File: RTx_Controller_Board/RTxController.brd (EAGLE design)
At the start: 101.6 x 85.5 mm, 73 parts

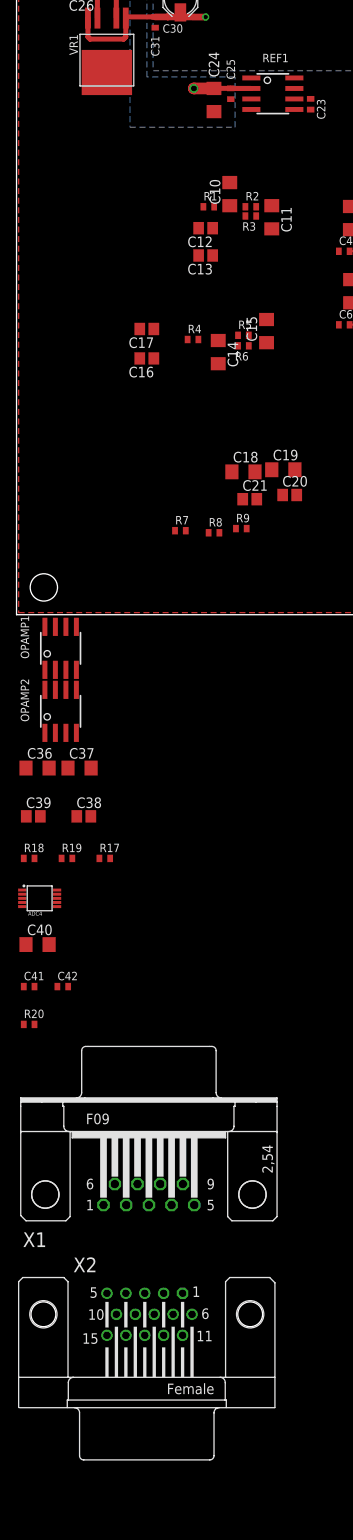
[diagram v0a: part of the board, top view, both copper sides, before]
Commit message: Changed ARef to 5.000V.
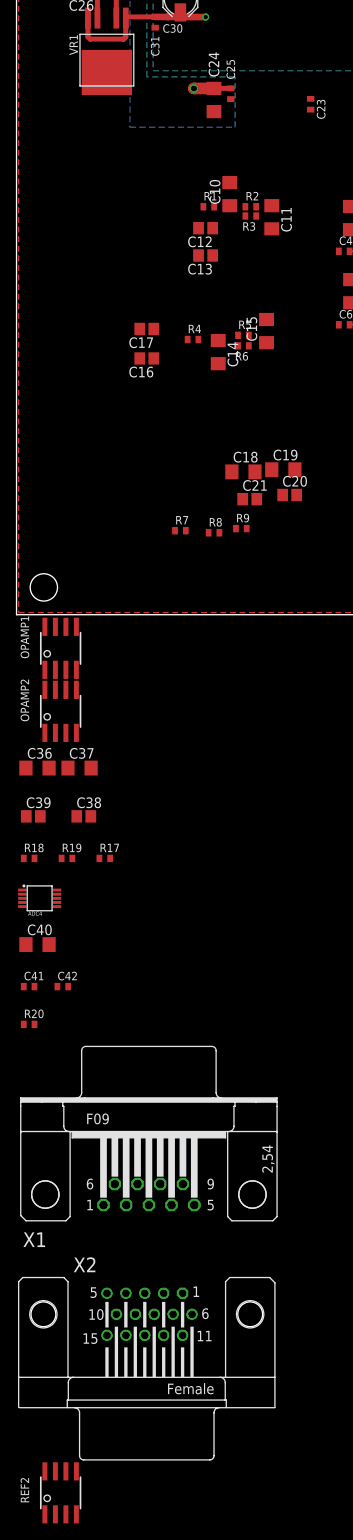
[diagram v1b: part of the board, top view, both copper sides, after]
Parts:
- removed REF1: ADR433RM-8, motorFeedback:SOIC8
- added REF2: ADR435RM-8, motorFeedback:SOIC8
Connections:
- removed net +3.000VREF: ADC1.1, ADC2.1, ADC3.1, ADC4.1, C1.2, C2.2, C23.1, C3.2, C40.2, R10.1, REF1.6
- new net +18V: C24.1, C25.1, REF2.2
- new net +5.000VREF: ADC1.1, ADC2.1, ADC3.1, ADC4.1, C1.2, C2.2, C23.1, C3.2, C40.2, R10.1, REF2.6
- net +5V: no longer C24.1, C25.1, REF1.2
- net GND: now also REF2.4; no longer REF1.4
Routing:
- net +5.000VREF: track 0.00 -> 7.47 mm
- net +3.000VREF: track 7.47 -> 0.00 mm
- net +5V: track 14.1 -> 7.19 mm, vias 2 -> 1
- net +18V: track 0.00 -> 4.49 mm, vias 0 -> 1
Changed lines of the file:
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@@
 <attribute name="NAME" x="42.796" y="42.858" size="0.5" layer="25" font="vector"/>
 </element>
-<element name="REF1" library="motorFeedback" package="SOIC8" value="ADR433RM-8" x="30.988" y="62.992" rot="R270"/>
 <element name="ADC2" library="motorFeedback" package="MSOP-10" value="AD7685RM-10" x="44.196" y="36.068"/>
 <element name="ADC3" library="motorFeedback" package="MSOP-10" value="AD7685RM-10" x="48.26" y="11.684"/>
@@
 <attribute name="OC_FARNELL" value="unknown" x="15.748" y="-84.582" size="1.778" layer="27" display="off"/>
 </element>
+<element name="REF2" library="motorFeedback" package="SOIC8" value="ADR435RM-8" x="5.334" y="-106.172"/>
 </elements>
 <signals>
@@
 <contactref element="ADC1" pad="4"/>
 <contactref element="ADC1" pad="5"/>
-<contactref element="REF1" pad="4"/>
 <contactref element="ADC2" pad="4"/>
 <contactref element="ADC2" pad="5"/>
@@
 <contactref element="ADC4" pad="5"/>
 <contactref element="ADC4" pad="4"/>
+<contactref element="REF2" pad="4"/>
 <wire x1="88.9" y1="59.944" x2="93.472" y2="63.83" width="0" layer="19" extent="1-1"/>
 <wire x1="88.9" y1="58.42" x2="88.9" y2="59.944" width="0" layer="19" extent="1-1"/>
@@
 <wire x1="46.228" y1="60.618" x2="74.676" y2="63.83" width="0" layer="19" extent="1-1"/>
 <wire x1="35.56" y1="61.072" x2="46.228" y2="60.618" width="0" layer="19" extent="1-1"/>
-<wire x1="28.388" y1="61.087" x2="35.56" y2="61.072" width="0" layer="19" extent="1-1"/>
-<wire x1="25.908" y1="62.342" x2="28.388" y2="61.087" width="0" layer="19" extent="1-1"/>
+<wire x1="25.908" y1="62.342" x2="35.56" y2="61.072" width="0" layer="19" extent="1-1"/>
 <wire x1="23.876" y1="60.83" x2="25.908" y2="62.342" width="0" layer="19" extent="1-1"/>
 <wire x1="25.781" y1="52.2508" x2="23.876" y2="60.83" width="0" layer="19" extent="1-1"/>
@@
 <wire x1="2.174" y1="-44.958" x2="1.14" y2="-39.878" width="0" layer="19" extent="1-1"/>
 <wire x1="6.238" y1="-44.958" x2="2.174" y2="-44.958" width="0" layer="19" extent="1-1"/>
+<wire x1="7.239" y1="-108.772" x2="6.238" y2="-44.958" width="0" layer="19" extent="1-1"/>
 </signal>
 <signal name="+5V">
 <contactref element="ADC1" pad="2"/>
-<contactref element="REF1" pad="2"/>
 <contactref element="C4" pad="1"/>
 <contactref element="C6" pad="1"/>
 <contactref element="C8" pad="1"/>
-<contactref element="C25" pad="1"/>
-<contactref element="C24" pad="1"/>
 <contactref element="VR1" pad="4"/>
 <contactref element="C26" pad="1"/>
@@
 <wire x1="9.779" y1="75.438" x2="9.54" y2="75.677" width="0.6096" layer="1" curve="-90"/>
 <wire x1="9.54" y1="75.677" x2="9.54" y2="77.597" width="0.6096" layer="1"/>
-<wire x1="23.876" y1="63.63" x2="25.908" y2="63.642" width="0.6096" layer="1"/>
-<wire x1="25.908" y1="63.642" x2="25.923" y2="63.627" width="0.6096" layer="1"/>
-<wire x1="25.923" y1="63.627" x2="28.388" y2="63.627" width="0.6096" layer="1"/>
-<wire x1="21.4406" y1="63.63" x2="23.876" y2="63.63" width="1.4224" layer="1"/>
-<wire x1="21.4376" y1="63.627" x2="21.4406" y2="63.63" width="1.4224" layer="1"/>
 <wire x1="9.54" y1="77.597" x2="9.54" y2="78.9536" width="0.6096" layer="1"/>
 <wire x1="9.54" y1="78.9536" x2="9.525" y2="78.9686" width="0.6096" layer="1"/>
-<via x="21.4376" y="63.627" extent="1-16" drill="0.7"/>
 <via x="9.525" y="78.9686" extent="1-16" drill="0.6"/>
 <polygon width="0.254" layer="16">
@@
 <wire x1="42.096" y1="36.568" x2="38.974" y2="43.942" width="0" layer="19" extent="1-1"/>
 <wire x1="38.974" y1="35.052" x2="42.096" y2="36.568" width="0" layer="19" extent="1-1"/>
-<wire x1="28.388" y1="63.627" x2="38.974" y2="43.942" width="0" layer="19" extent="1-1"/>
-<wire x1="9.779" y1="72.136" x2="21.4406" y2="63.63" width="0" layer="19" extent="1-1"/>
 <wire x1="46.16" y1="12.184" x2="38.974" y2="35.052" width="0" layer="19" extent="1-1"/>
 <wire x1="43.038" y1="10.668" x2="46.16" y2="12.184" width="0" layer="19" extent="1-1"/>
+<wire x1="9.779" y1="72.136" x2="38.974" y2="43.942" width="0" layer="19" extent="1-1"/>
 <wire x1="3.429" y1="-1.464" x2="43.038" y2="10.668" width="0" layer="19" extent="1-1"/>
 <wire x1="0.694" y1="-33.79" x2="3.429" y2="-1.464" width="0" layer="19" extent="1-1"/>
 <wire x1="0.874" y1="-44.958" x2="0.694" y2="-33.79" width="0" layer="19" extent="1-1"/>
-</signal>
-<signal name="+3.000VREF">
-<contactref element="ADC1" pad="1"/>
-<contactref element="ADC2" pad="1"/>
-<contactref element="ADC3" pad="1"/>
-<contactref element="C1" pad="2"/>
-<contactref element="C2" pad="2"/>
-<contactref element="C3" pad="2"/>
-<contactref element="REF1" pad="6"/>
-<contactref element="R10" pad="1"/>
-<contactref element="C23" pad="1"/>
-<wire x1="40.386" y1="37.068" x2="42.096" y2="37.068" width="0.254" layer="1"/>
-<wire x1="40.386" y1="37.716" x2="40.386" y2="37.068" width="0.254" layer="1"/>
-<wire x1="44.45" y1="12.684" x2="46.16" y2="12.684" width="0.254" layer="1"/>
-<wire x1="44.45" y1="12.684" x2="44.45" y2="13.332" width="0.254" layer="1"/>
-<wire x1="40.402" y1="45.958" x2="42.096" y2="45.958" width="0.254" layer="1"/>
-<wire x1="40.386" y1="45.974" x2="40.402" y2="45.958" width="0.254" layer="1"/>
-<wire x1="40.386" y1="46.7838" x2="40.386" y2="45.974" width="0.254" layer="1"/>
-<wire x1="40.3606" y1="46.5552" x2="40.386" y2="46.7838" width="0.254" layer="1"/>
-<contactref element="C40" pad="2"/>
-<contactref element="ADC4" pad="1"/>
-<wire x1="35.56" y1="62.372" x2="42.9872" y2="62.357" width="0" layer="19" extent="1-1"/>
-<wire x1="33.588" y1="62.357" x2="35.56" y2="62.372" width="0" layer="19" extent="1-1"/>
-<wire x1="40.386" y1="46.7838" x2="42.9872" y2="62.357" width="0" layer="19" extent="1-1"/>
-<wire x1="40.386" y1="37.716" x2="40.402" y2="45.958" width="0" layer="19" extent="1-1"/>
-<wire x1="44.45" y1="13.332" x2="42.096" y2="37.068" width="0" layer="19" extent="1-1"/>
-<wire x1="0.694" y1="-33.29" x2="44.45" y2="12.684" width="0" layer="19" extent="1-1"/>
-<wire x1="3.94" y1="-39.878" x2="0.694" y2="-33.29" width="0" layer="19" extent="1-1"/>
 </signal>
 <signal name="CNV">
@@
 <wire x1="4.894" y1="-34.79" x2="0.874" y2="-49.53" width="0" layer="19" extent="1-1"/>
 </signal>
+<signal name="+5.000VREF">
+<contactref element="R10" pad="1"/>
+<contactref element="C23" pad="1"/>
+<contactref element="ADC1" pad="1"/>
+<contactref element="C1" pad="2"/>
+<wire x1="40.402" y1="45.958" x2="42.096" y2="45.958" width="0.254" layer="1"/>
+<wire x1="40.386" y1="45.974" x2="40.402" y2="45.958" width="0.254" layer="1"/>
+<wire x1="40.386" y1="46.7838" x2="40.386" y2="45.974" width="0.254" layer="1"/>
+<wire x1="40.3606" y1="46.5552" x2="40.386" y2="46.7838" width="0.254" layer="1"/>
+<contactref element="ADC2" pad="1"/>
+<contactref element="C2" pad="2"/>
+<wire x1="40.386" y1="37.068" x2="42.096" y2="37.068" width="0.254" layer="1"/>
+<wire x1="40.386" y1="37.716" x2="40.386" y2="37.068" width="0.254" layer="1"/>
+<contactref element="ADC3" pad="1"/>
+<contactref element="C3" pad="2"/>
+<wire x1="44.45" y1="12.684" x2="46.16" y2="12.684" width="0.254" layer="1"/>
+<wire x1="44.45" y1="12.684" x2="44.45" y2="13.332" width="0.254" layer="1"/>
+<contactref element="C40" pad="2"/>
+<contactref element="ADC4" pad="1"/>
+<contactref element="REF2" pad="6"/>
+<wire x1="35.56" y1="62.372" x2="42.9872" y2="62.357" width="0" layer="19" extent="1-1"/>
+<wire x1="40.386" y1="46.7838" x2="42.9872" y2="62.357" width="0" layer="19" extent="1-1"/>
+<wire x1="40.386" y1="37.716" x2="40.402" y2="45.958" width="0" layer="19" extent="1-1"/>
+<wire x1="44.45" y1="13.332" x2="42.096" y2="37.068" width="0" layer="19" extent="1-1"/>
+<wire x1="0.694" y1="-33.29" x2="44.45" y2="12.684" width="0" layer="19" extent="1-1"/>
+<wire x1="3.94" y1="-39.878" x2="0.694" y2="-33.29" width="0" layer="19" extent="1-1"/>
+<wire x1="5.969" y1="-103.572" x2="3.94" y2="-39.878" width="0" layer="19" extent="1-1"/>
+</signal>
+<signal name="+18V">
+<contactref element="C25" pad="1"/>
+<contactref element="C24" pad="1"/>
+<contactref element="REF2" pad="2"/>
+<wire x1="23.876" y1="63.63" x2="25.908" y2="63.642" width="0.6096" layer="1"/>
+<wire x1="25.908" y1="63.642" x2="25.923" y2="63.627" width="0.6096" layer="1"/>
+<wire x1="21.4406" y1="63.63" x2="23.876" y2="63.63" width="1.4224" layer="1"/>
+<wire x1="21.4376" y1="63.627" x2="21.4406" y2="63.63" width="1.4224" layer="1"/>
+<via x="21.4376" y="63.627" extent="1-16" drill="0.7"/>
+<wire x1="21.4406" y1="63.63" x2="4.699" y2="-108.772" width="0" layer="19" extent="1-1"/>
+</signal>
 </signals>

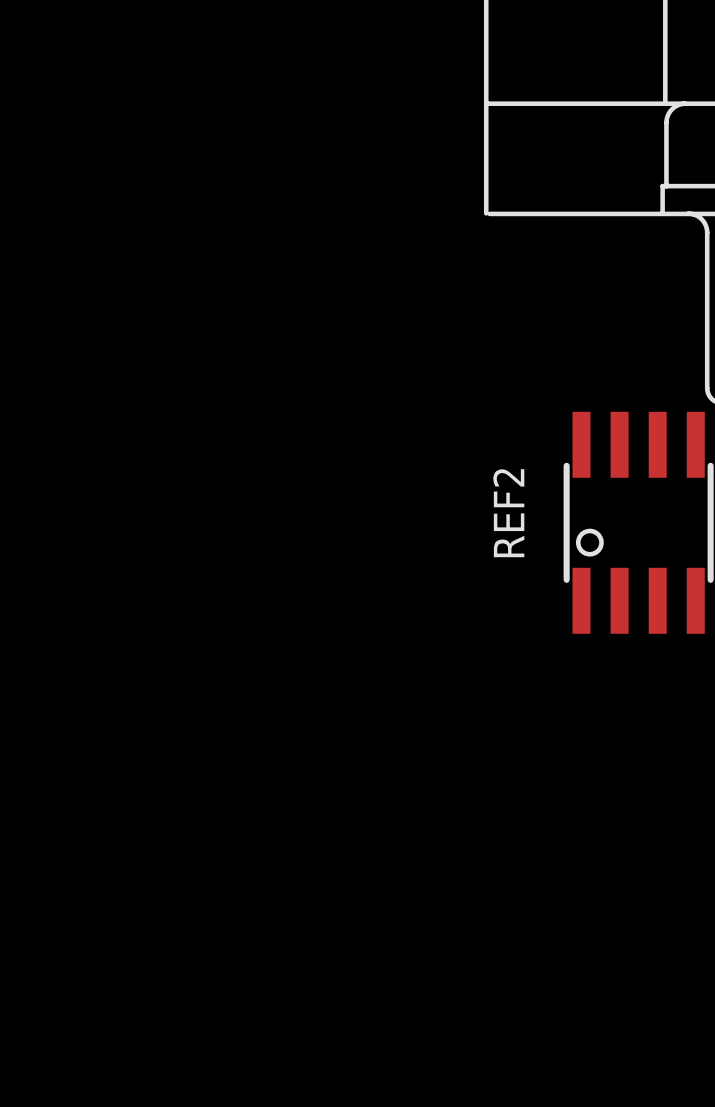
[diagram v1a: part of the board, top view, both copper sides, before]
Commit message: Initial check-in datasheet for USB ESD protection. Added initial USB setup to schematic.
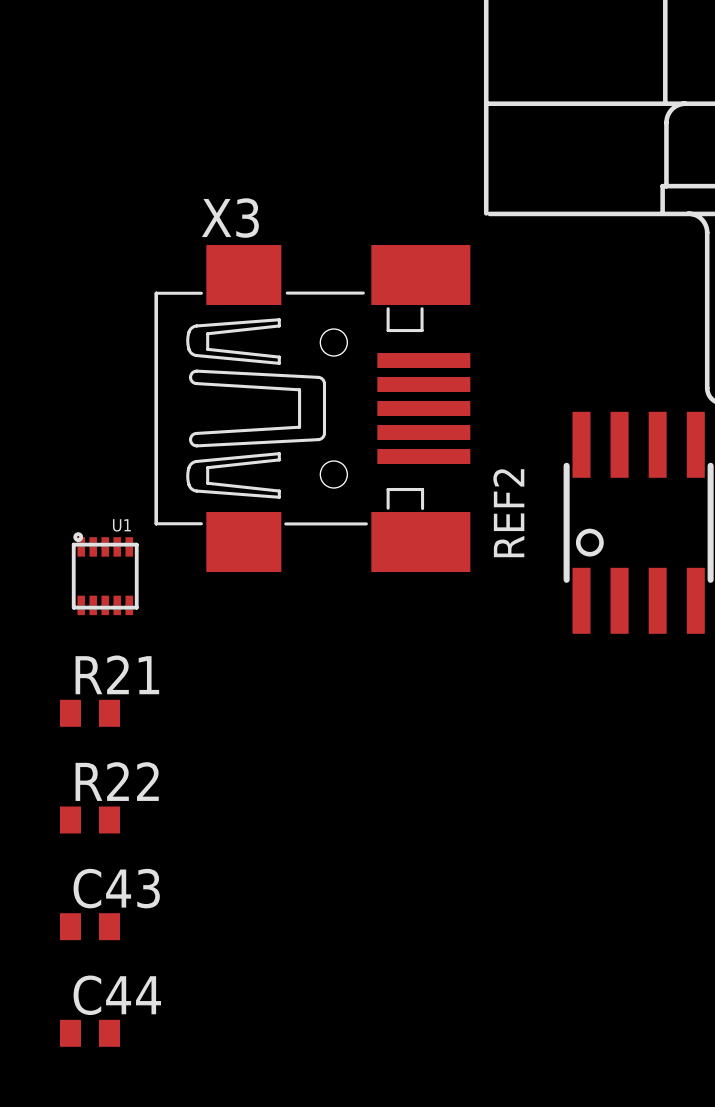
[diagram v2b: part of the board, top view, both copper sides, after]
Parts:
- added C43, C44: 10u, rcl:C0402
- added R21, R22: 22, rcl:R0402
- added U1: TPD4S014, rtx:TPD4S014
- added X3: MINI-USB-32005-301, con-cypressindustries:32005-301
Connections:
- new net D+: R21.1, U1.7, X3.2
- new net D-: R22.1, U1.6, X3.3
- new net PA11/D-: R22.2
- new net PA12/D+: R21.2
- new net PA9/VBUS: C44.1, U1.1
- net +5V: now also C43.1, U1.9, X3.1
- net GND: now also C43.2, C44.2, U1.5, U1.8, X3.4, X3.5
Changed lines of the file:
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@@
 </element>
 <element name="REF2" library="motorFeedback" package="SOIC8" value="ADR435RM-8" x="5.334" y="-106.172"/>
+<element name="X3" library="con-cypressindustries" package="32005-301" value="MINI-USB-32005-301" x="-4.826" y="-102.362">
+<attribute name="OC_NEWARK" value="unknown" x="-4.826" y="-102.362" size="1.778" layer="27" display="off"/>
+<attribute name="MPN" value="" x="-4.826" y="-102.362" size="1.778" layer="27" display="off"/>
+<attribute name="MF" value="" x="-4.826" y="-102.362" size="1.778" layer="27" display="off"/>
+<attribute name="OC_FARNELL" value="unknown" x="-4.826" y="-102.362" size="1.778" layer="27" display="off"/>
+</element>
+<element name="U1" library="rtx" package="TPD4S014" value="TPD4S014" x="-12.446" y="-107.95"/>
+<element name="R21" library="rcl" package="R0402" value="22" x="-12.954" y="-112.522"/>
+<element name="R22" library="rcl" package="R0402" value="22" x="-12.954" y="-116.078"/>
+<element name="C43" library="rcl" package="C0402" value="10u" x="-12.954" y="-119.634"/>
+<element name="C44" library="rcl" package="C0402" value="10u" x="-12.954" y="-123.19"/>
 </elements>
 <signals>
@@
 <contactref element="ADC4" pad="4"/>
 <contactref element="REF2" pad="4"/>
+<contactref element="X3" pad="4"/>
+<contactref element="X3" pad="5"/>
+<contactref element="U1" pad="5"/>
+<contactref element="U1" pad="8"/>
+<contactref element="C43" pad="2"/>
+<contactref element="C44" pad="2"/>
 <wire x1="88.9" y1="59.944" x2="93.472" y2="63.83" width="0" layer="19" extent="1-1"/>
 <wire x1="88.9" y1="58.42" x2="88.9" y2="59.944" width="0" layer="19" extent="1-1"/>
@@
 <wire x1="2.174" y1="-44.958" x2="1.14" y2="-39.878" width="0" layer="19" extent="1-1"/>
 <wire x1="6.238" y1="-44.958" x2="2.174" y2="-44.958" width="0" layer="19" extent="1-1"/>
-<wire x1="7.239" y1="-108.772" x2="6.238" y2="-44.958" width="0" layer="19" extent="1-1"/>
+<wire x1="-1.826" y1="-103.162" x2="2.174" y2="-44.958" width="0" layer="19" extent="1-1"/>
+<wire x1="-1.826" y1="-103.962" x2="-1.826" y2="-103.162" width="0" layer="19" extent="1-1"/>
+<wire x1="7.239" y1="-108.772" x2="-1.826" y2="-103.962" width="0" layer="19" extent="1-1"/>
+<wire x1="-11.646" y1="-106.975" x2="-1.826" y2="-103.962" width="0" layer="19" extent="1-1"/>
+<wire x1="-12.446" y1="-108.925" x2="-11.646" y2="-106.975" width="0" layer="19" extent="1-1"/>
+<wire x1="-12.304" y1="-119.634" x2="-12.446" y2="-108.925" width="0" layer="19" extent="1-1"/>
+<wire x1="-12.304" y1="-123.19" x2="-12.304" y2="-119.634" width="0" layer="19" extent="1-1"/>
 </signal>
 <signal name="+5V">
@@
 <contactref element="C41" pad="1"/>
 <contactref element="ADC4" pad="2"/>
-<wire x1="38.974" y1="43.942" x2="42.096" y2="45.458" width="0" layer="19" extent="1-1"/>
-<wire x1="42.096" y1="36.568" x2="38.974" y2="43.942" width="0" layer="19" extent="1-1"/>
-<wire x1="38.974" y1="35.052" x2="42.096" y2="36.568" width="0" layer="19" extent="1-1"/>
-<wire x1="46.16" y1="12.184" x2="38.974" y2="35.052" width="0" layer="19" extent="1-1"/>
-<wire x1="43.038" y1="10.668" x2="46.16" y2="12.184" width="0" layer="19" extent="1-1"/>
+<contactref element="X3" pad="1"/>
+<contactref element="C43" pad="1"/>
+<contactref element="U1" pad="9"/>
+<wire x1="-12.846" y1="-108.925" x2="-13.604" y2="-119.634" width="0" layer="19" extent="1-1"/>
+<wire x1="-1.826" y1="-100.762" x2="-12.846" y2="-108.925" width="0" layer="19" extent="1-1"/>
+<wire x1="0.874" y1="-44.958" x2="-1.826" y2="-100.762" width="0" layer="19" extent="1-1"/>
+<wire x1="0.694" y1="-33.79" x2="0.874" y2="-44.958" width="0" layer="19" extent="1-1"/>
+<wire x1="3.429" y1="-1.464" x2="0.694" y2="-33.79" width="0" layer="19" extent="1-1"/>
+<wire x1="43.038" y1="10.668" x2="3.429" y2="-1.464" width="0" layer="19" extent="1-1"/>
+<wire x1="46.16" y1="12.184" x2="43.038" y2="10.668" width="0" layer="19" extent="1-1"/>
+<wire x1="38.974" y1="35.052" x2="46.16" y2="12.184" width="0" layer="19" extent="1-1"/>
+<wire x1="42.096" y1="36.568" x2="38.974" y2="35.052" width="0" layer="19" extent="1-1"/>
+<wire x1="38.974" y1="43.942" x2="42.096" y2="36.568" width="0" layer="19" extent="1-1"/>
+<wire x1="42.096" y1="45.458" x2="38.974" y2="43.942" width="0" layer="19" extent="1-1"/>
 <wire x1="9.779" y1="72.136" x2="38.974" y2="43.942" width="0" layer="19" extent="1-1"/>
-<wire x1="3.429" y1="-1.464" x2="43.038" y2="10.668" width="0" layer="19" extent="1-1"/>
-<wire x1="0.694" y1="-33.79" x2="3.429" y2="-1.464" width="0" layer="19" extent="1-1"/>
-<wire x1="0.874" y1="-44.958" x2="0.694" y2="-33.79" width="0" layer="19" extent="1-1"/>
 </signal>
 <signal name="CNV">
@@
 <wire x1="21.4406" y1="63.63" x2="4.699" y2="-108.772" width="0" layer="19" extent="1-1"/>
 </signal>
+<signal name="D+">
+<contactref element="X3" pad="2"/>
+<contactref element="U1" pad="7"/>
+<contactref element="R21" pad="1"/>
+<wire x1="-12.046" y1="-108.925" x2="-13.604" y2="-112.522" width="0" layer="19" extent="1-1"/>
+<wire x1="-1.826" y1="-101.562" x2="-12.046" y2="-108.925" width="0" layer="19" extent="1-1"/>
+</signal>
+<signal name="D-">
+<contactref element="X3" pad="3"/>
+<contactref element="U1" pad="6"/>
+<contactref element="R22" pad="1"/>
+<wire x1="-11.646" y1="-108.925" x2="-13.604" y2="-116.078" width="0" layer="19" extent="1-1"/>
+<wire x1="-1.826" y1="-102.362" x2="-11.646" y2="-108.925" width="0" layer="19" extent="1-1"/>
+</signal>
+<signal name="PA9/VBUS">
+<contactref element="U1" pad="1"/>
+<contactref element="C44" pad="1"/>
+<wire x1="-13.246" y1="-106.975" x2="-13.604" y2="-123.19" width="0" layer="19" extent="1-1"/>
+</signal>
+<signal name="PA12/D+">
+<contactref element="R21" pad="2"/>
+</signal>
+<signal name="PA11/D-">
+<contactref element="R22" pad="2"/>
+</signal>
 </signals>
